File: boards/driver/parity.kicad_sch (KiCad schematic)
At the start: 11 parts, among them Q88 MMBT2222, Q89 MMBT2222

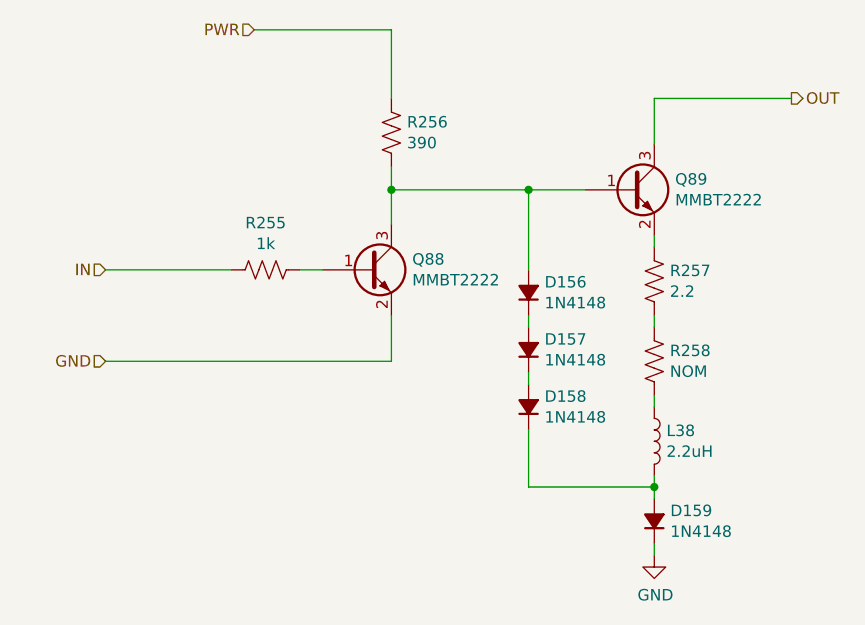
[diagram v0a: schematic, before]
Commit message: Driver: Added a 5V->3.3V LDO to replace the reversed cmod header, added jumpers for the 200R parallel returns, and renamed subcircuit ports to avoid unexpected ground connections.
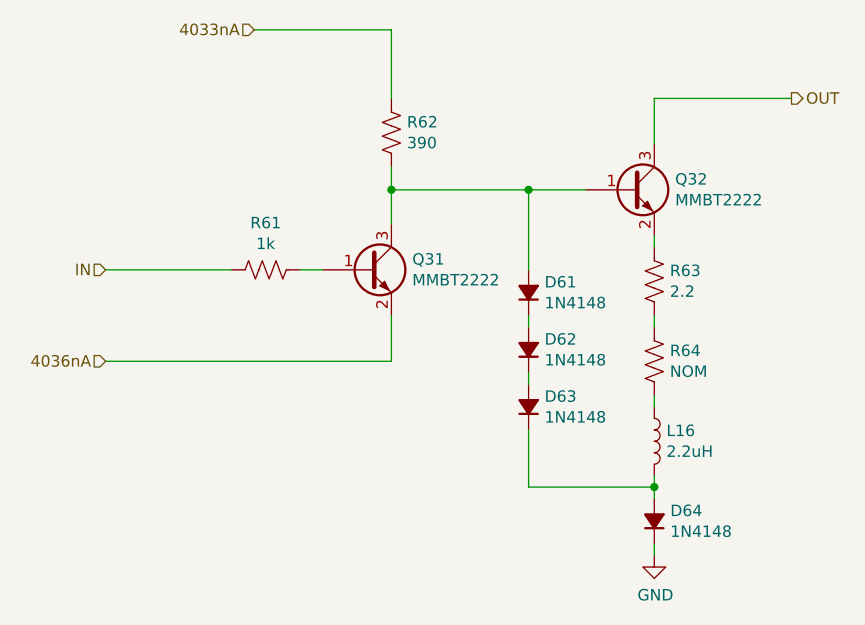
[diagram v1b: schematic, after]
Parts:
- renumbered D156 to D61, D157 to D62, D158 to D63, D159 to D64, L38 to L16, Q88 to Q31, Q89 to Q32, R255 to R61, R256 to R62, R257 to R63, R258 to R64
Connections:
- net GND: no longer Q31.2 (E)
- net PWR renamed 4033nA
- new net 4036nA: Q31.2 (E)
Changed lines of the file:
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@@
     (stroke (width 0) (type default) (color 0 0 0 0))
   )
-  (hierarchical_label "GND" (shape input) (at 95.25 104.14 180)
+  (hierarchical_label "4036nA" (shape input) (at 95.25 104.14 180)
     (effects (font (size 1.27 1.27)) (justify right))
   )
@@
     (effects (font (size 1.27 1.27)) (justify left))
   )
-  (hierarchical_label "PWR" (shape input) (at 111.76 67.31 180)
+  (hierarchical_label "4033nA" (shape input) (at 111.76 67.31 180)
     (effects (font (size 1.27 1.27)) (justify right))
   )
@@
   (symbol (lib_id "Device:R_US") (at 113.03 93.98 270)
     (in_bom yes) (on_board yes)
-    (property "Reference" "R255" (id 0) (at 113.03 88.773 90))
+    (property "Reference" "R61" (id 0) (at 113.03 88.773 90))
     (property "Value" "1k" (id 1) (at 113.03 91.0844 90))
     (property "Footprint" "Resistor_SMD:R_0603_1608Metric" (id 2) (at 112.776 94.996 90)
@@
   (symbol (lib_id "Device:Q_NPN_BEC") (at 124.46 93.98 0)
     (in_bom yes) (on_board yes)
-    (property "Reference" "Q88" (id 0) (at 129.3114 92.8116 0)
+    (property "Reference" "Q31" (id 0) (at 129.3114 92.8116 0)
       (effects (font (size 1.27 1.27)) (justify left))
     )
@@
   (symbol (lib_id "Device:D_Small_Filled") (at 142.24 109.22 90)
     (in_bom yes) (on_board yes)
-    (property "Reference" "D158" (id 0) (at 144.018 108.0516 90)
+    (property "Reference" "D63" (id 0) (at 144.018 108.0516 90)
       (effects (font (size 1.27 1.27)) (justify right))
     )
@@
   (symbol (lib_id "Device:D_Small_Filled") (at 142.24 102.87 90)
     (in_bom yes) (on_board yes)
-    (property "Reference" "D157" (id 0) (at 144.018 101.7016 90)
+    (property "Reference" "D62" (id 0) (at 144.018 101.7016 90)
       (effects (font (size 1.27 1.27)) (justify right))
     )
@@
   (symbol (lib_id "Device:D_Small_Filled") (at 142.24 96.52 90)
     (in_bom yes) (on_board yes)
-    (property "Reference" "D156" (id 0) (at 144.018 95.3516 90)
+    (property "Reference" "D61" (id 0) (at 144.018 95.3516 90)
       (effects (font (size 1.27 1.27)) (justify right))
     )
@@
   (symbol (lib_id "Device:Q_NPN_BEC") (at 153.67 85.09 0)
     (in_bom yes) (on_board yes)
-    (property "Reference" "Q89" (id 0) (at 158.5214 83.9216 0)
+    (property "Reference" "Q32" (id 0) (at 158.5214 83.9216 0)
       (effects (font (size 1.27 1.27)) (justify left))
     )
@@
   (symbol (lib_id "Device:R_US") (at 156.21 95.25 0)
     (in_bom yes) (on_board yes)
-    (property "Reference" "R257" (id 0) (at 157.9372 94.0816 0)
+    (property "Reference" "R63" (id 0) (at 157.9372 94.0816 0)
       (effects (font (size 1.27 1.27)) (justify left))
     )
@@
   (symbol (lib_id "Device:R_US") (at 127 78.74 0)
     (in_bom yes) (on_board yes)
-    (property "Reference" "R256" (id 0) (at 128.7272 77.5716 0)
+    (property "Reference" "R62" (id 0) (at 128.7272 77.5716 0)
       (effects (font (size 1.27 1.27)) (justify left))
     )
@@
   (symbol (lib_id "Device:R_US") (at 156.21 104.14 0)
     (in_bom yes) (on_board yes)
-    (property "Reference" "R258" (id 0) (at 157.9372 102.9716 0)
+    (property "Reference" "R64" (id 0) (at 157.9372 102.9716 0)
       (effects (font (size 1.27 1.27)) (justify left))
     )
@@
   (symbol (lib_id "Device:D_Small_Filled") (at 156.21 121.92 90)
     (in_bom yes) (on_board yes)
-    (property "Reference" "D159" (id 0) (at 157.988 120.7516 90)
+    (property "Reference" "D64" (id 0) (at 157.988 120.7516 90)
       (effects (font (size 1.27 1.27)) (justify right))
     )
@@
   (symbol (lib_id "Device:L") (at 156.21 113.03 0)
     (in_bom yes) (on_board yes)
-    (property "Reference" "L38" (id 0) (at 157.5562 111.8616 0)
+    (property "Reference" "L16" (id 0) (at 157.5562 111.8616 0)
       (effects (font (size 1.27 1.27)) (justify left))
     )
@@
   (symbol (lib_id "power:GND") (at 156.21 125.73 0)
     (in_bom yes) (on_board yes)
-    (property "Reference" "#PWR0126" (id 0) (at 156.21 132.08 0)
-      (effects (font (size 1.27 1.27)) hide)
-    )
+    (property "Reference" "#PWR016" (id 0) (at 156.21 132.08 0)
+      (effects (font (size 1.27 1.27)) hide)
+    )

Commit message: Driver: incorporated most changes from the test board, and began layout
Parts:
- D29: renamed from D61; footprint Diode_SMD:D_SOD-323 -> lachesis:D_SOD-323
- D30: renamed from D62; footprint Diode_SMD:D_SOD-323 -> lachesis:D_SOD-323
- D31: renamed from D63; footprint Diode_SMD:D_SOD-323 -> lachesis:D_SOD-323
- D32: renamed from D64; footprint Diode_SMD:D_SOD-323 -> lachesis:D_SOD-323
- L8: renamed from L16; footprint Inductor_SMD:L_1812_4532Metric -> lachesis:API_Delevan_1812R
- renumbered Q31 to Q15, Q32 to Q16, R61 to R29, R62 to R30, R63 to R31, R64 to R32
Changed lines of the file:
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@@
     (effects (font (size 1.27 1.27)) (justify right))
   )
-  (symbol (lib_id "Device:R_US") (at 113.03 93.98 270)
-    (in_bom yes) (on_board yes)
-    (property "Reference" "R61" (id 0) (at 113.03 88.773 90))
+  (symbol (lib_id "Device:R_US") (at 113.03 93.98 270) (unit 1)
+    (in_bom yes) (on_board yes)
+    (property "Reference" "R29" (id 0) (at 113.03 88.773 90))
     (property "Value" "1k" (id 1) (at 113.03 91.0844 90))
     (property "Footprint" "Resistor_SMD:R_0603_1608Metric" (id 2) (at 112.776 94.996 90)
@@
     (pin "2")
   )
-  (symbol (lib_id "Device:Q_NPN_BEC") (at 124.46 93.98 0)
-    (in_bom yes) (on_board yes)
-    (property "Reference" "Q31" (id 0) (at 129.3114 92.8116 0)
+  (symbol (lib_id "Device:Q_NPN_BEC") (at 124.46 93.98 0) (unit 1)
+    (in_bom yes) (on_board yes)
+    (property "Reference" "Q15" (id 0) (at 129.3114 92.8116 0)
       (effects (font (size 1.27 1.27)) (justify left))
     )
@@
     (pin "3")
   )
-  (symbol (lib_id "Device:D_Small_Filled") (at 142.24 109.22 90)
-    (in_bom yes) (on_board yes)
-    (property "Reference" "D63" (id 0) (at 144.018 108.0516 90)
+  (symbol (lib_id "Device:D_Small_Filled") (at 142.24 109.22 90) (unit 1)
+    (in_bom yes) (on_board yes)
+    (property "Reference" "D31" (id 0) (at 144.018 108.0516 90)
       (effects (font (size 1.27 1.27)) (justify right))
     )
@@
       (effects (font (size 1.27 1.27)) (justify right))
     )
-    (property "Footprint" "Diode_SMD:D_SOD-323" (id 2) (at 142.24 109.22 90)
+    (property "Footprint" "lachesis:D_SOD-323" (id 2) (at 142.24 109.22 90)
       (effects (font (size 1.27 1.27)) hide)
     )
@@
     (pin "2")
   )
-  (symbol (lib_id "Device:D_Small_Filled") (at 142.24 102.87 90)
-    (in_bom yes) (on_board yes)
-    (property "Reference" "D62" (id 0) (at 144.018 101.7016 90)
+  (symbol (lib_id "Device:D_Small_Filled") (at 142.24 102.87 90) (unit 1)
+    (in_bom yes) (on_board yes)
+    (property "Reference" "D30" (id 0) (at 144.018 101.7016 90)
       (effects (font (size 1.27 1.27)) (justify right))
     )
@@
       (effects (font (size 1.27 1.27)) (justify right))
     )
-    (property "Footprint" "Diode_SMD:D_SOD-323" (id 2) (at 142.24 102.87 90)
+    (property "Footprint" "lachesis:D_SOD-323" (id 2) (at 142.24 102.87 90)
       (effects (font (size 1.27 1.27)) hide)
     )
@@
     (pin "2")
   )
-  (symbol (lib_id "Device:D_Small_Filled") (at 142.24 96.52 90)
-    (in_bom yes) (on_board yes)
-    (property "Reference" "D61" (id 0) (at 144.018 95.3516 90)
+  (symbol (lib_id "Device:D_Small_Filled") (at 142.24 96.52 90) (unit 1)
+    (in_bom yes) (on_board yes)
+    (property "Reference" "D29" (id 0) (at 144.018 95.3516 90)
       (effects (font (size 1.27 1.27)) (justify right))
     )
@@
       (effects (font (size 1.27 1.27)) (justify right))
     )
-    (property "Footprint" "Diode_SMD:D_SOD-323" (id 2) (at 142.24 96.52 90)
+    (property "Footprint" "lachesis:D_SOD-323" (id 2) (at 142.24 96.52 90)
       (effects (font (size 1.27 1.27)) hide)
     )
@@
     (pin "2")
   )
-  (symbol (lib_id "Device:Q_NPN_BEC") (at 153.67 85.09 0)
-    (in_bom yes) (on_board yes)
-    (property "Reference" "Q32" (id 0) (at 158.5214 83.9216 0)
+  (symbol (lib_id "Device:Q_NPN_BEC") (at 153.67 85.09 0) (unit 1)
+    (in_bom yes) (on_board yes)
+    (property "Reference" "Q16" (id 0) (at 158.5214 83.9216 0)
       (effects (font (size 1.27 1.27)) (justify left))
     )
@@
     (pin "3")
   )
-  (symbol (lib_id "Device:R_US") (at 156.21 95.25 0)
-    (in_bom yes) (on_board yes)
-    (property "Reference" "R63" (id 0) (at 157.9372 94.0816 0)
+  (symbol (lib_id "Device:R_US") (at 156.21 95.25 0) (unit 1)
+    (in_bom yes) (on_board yes)
+    (property "Reference" "R31" (id 0) (at 157.9372 94.0816 0)
       (effects (font (size 1.27 1.27)) (justify left))
     )
@@
     (pin "2")
   )
-  (symbol (lib_id "Device:R_US") (at 127 78.74 0)
-    (in_bom yes) (on_board yes)
-    (property "Reference" "R62" (id 0) (at 128.7272 77.5716 0)
+  (symbol (lib_id "Device:R_US") (at 127 78.74 0) (unit 1)
+    (in_bom yes) (on_board yes)
+    (property "Reference" "R30" (id 0) (at 128.7272 77.5716 0)
       (effects (font (size 1.27 1.27)) (justify left))
     )
@@
     (pin "2")
   )
-  (symbol (lib_id "Device:R_US") (at 156.21 104.14 0)
-    (in_bom yes) (on_board yes)
-    (property "Reference" "R64" (id 0) (at 157.9372 102.9716 0)
+  (symbol (lib_id "Device:R_US") (at 156.21 104.14 0) (unit 1)
+    (in_bom yes) (on_board yes)
+    (property "Reference" "R32" (id 0) (at 157.9372 102.9716 0)
       (effects (font (size 1.27 1.27)) (justify left))
     )
@@
     (pin "2")
   )
-  (symbol (lib_id "Device:D_Small_Filled") (at 156.21 121.92 90)
-    (in_bom yes) (on_board yes)
-    (property "Reference" "D64" (id 0) (at 157.988 120.7516 90)
+  (symbol (lib_id "Device:D_Small_Filled") (at 156.21 121.92 90) (unit 1)
+    (in_bom yes) (on_board yes)
+    (property "Reference" "D32" (id 0) (at 157.988 120.7516 90)
       (effects (font (size 1.27 1.27)) (justify right))
     )
@@
       (effects (font (size 1.27 1.27)) (justify right))
     )
-    (property "Footprint" "Diode_SMD:D_SOD-323" (id 2) (at 156.21 121.92 90)
+    (property "Footprint" "lachesis:D_SOD-323" (id 2) (at 156.21 121.92 90)
       (effects (font (size 1.27 1.27)) hide)
     )
@@
     (pin "2")
   )
-  (symbol (lib_id "Device:L") (at 156.21 113.03 0)
-    (in_bom yes) (on_board yes)
-    (property "Reference" "L16" (id 0) (at 157.5562 111.8616 0)
+  (symbol (lib_id "Device:L") (at 156.21 113.03 0) (unit 1)
+    (in_bom yes) (on_board yes)
+    (property "Reference" "L8" (id 0) (at 157.5562 111.8616 0)
       (effects (font (size 1.27 1.27)) (justify left))
     )
@@
       (effects (font (size 1.27 1.27)) (justify left))
     )
-    (property "Footprint" "Inductor_SMD:L_1812_4532Metric" (id 2) (at 156.21 113.03 0)
+    (property "Footprint" "lachesis:API_Delevan_1812R" (id 2) (at 156.21 113.03 0)
       (effects (font (size 1.27 1.27)) hide)
     )
@@
     (pin "2")
   )
-  (symbol (lib_id "power:GND") (at 156.21 125.73 0)
-    (in_bom yes) (on_board yes)
-    (property "Reference" "#PWR016" (id 0) (at 156.21 132.08 0)
-      (effects (font (size 1.27 1.27)) hide)
-    )
+  (symbol (lib_id "power:GND") (at 156.21 125.73 0) (unit 1)
+    (in_bom yes) (on_board yes)
+    (property "Reference" "#PWR08" (id 0) (at 156.21 132.08 0)
+      (effects (font (size 1.27 1.27)) hide)
+    )
